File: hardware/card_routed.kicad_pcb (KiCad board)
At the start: 2 copper layers, 143 x 80 mm, 1 part

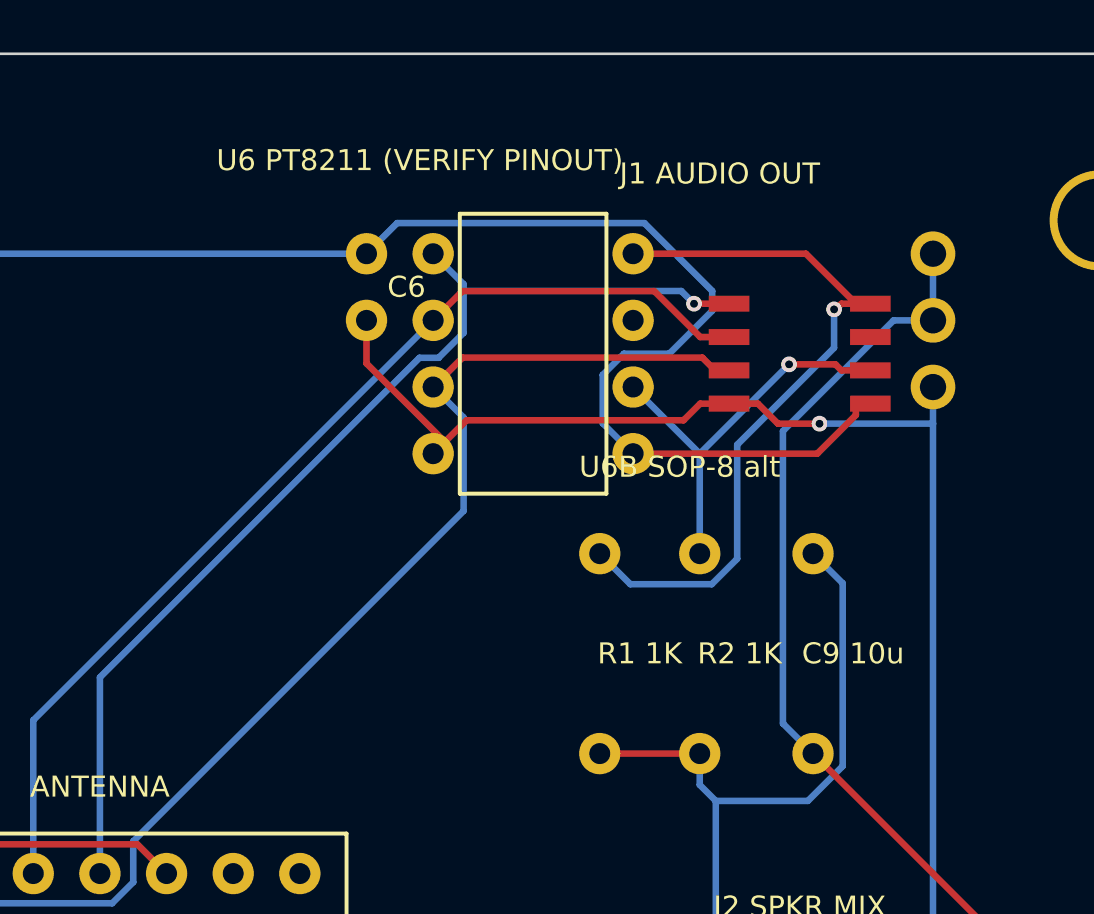
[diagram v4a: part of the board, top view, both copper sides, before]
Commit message: PT8211 datasheet in-tree; pinout verified and corrected
PT8211-S.pdf (Princeton Technology, v1.1) added to hardware/. The
flagged from-memory pinout was right on 6 of 8 pins: 6/8 were L/R
swapped (harmless — both sum to mono) and are now labeled truthfully
(6=LCH, 8=RCH, 7=NC). Datasheet also confirms both packages exist
(PT8211 DIP-8 / PT8211-S SO-8, matching our dual position) and that
the serial format is Japanese/LSB-justified, NOT standard I2S — noted
as a firmware requirement. 3.3V operation noted as Pico-ecosystem
practice vs the 5V nominal. Re-routed, DRC 0/0; fab package
regenerated. The last pre-order human check is closed.

Co-Authored-By: Claude Fable 5 <noreply@anthropic.com>
Claude-Session: https://claude.ai/code/session_01PB6zhL6oFB9zbtD4W85UDt
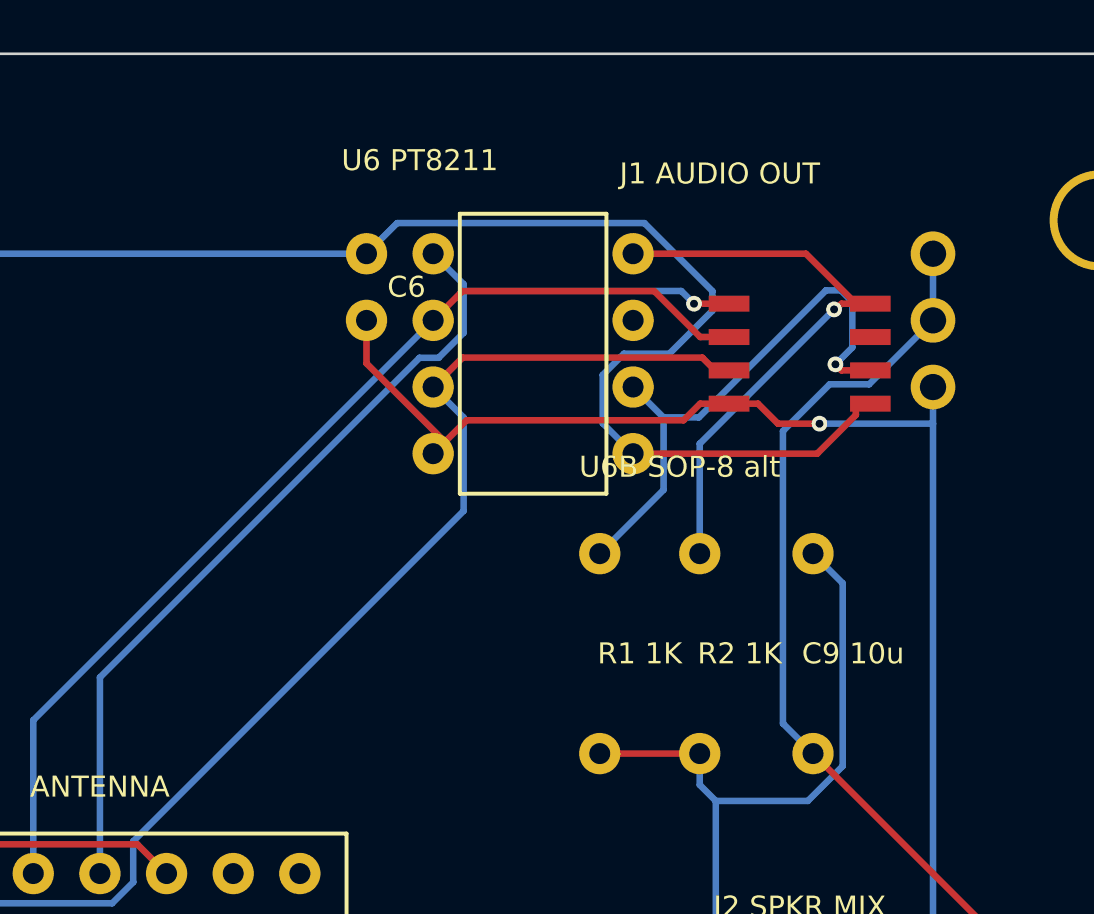
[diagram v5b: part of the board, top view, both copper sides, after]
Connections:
- ? pad 122: AOL -> AOR
- ? pad 126: AOR -> AOL
- ? pad 130: AOL -> AOR
- ? pad 134: AOR -> AOL
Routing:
- net AOR: track 15.4 -> 22.2 mm
- net AOL: track 27.9 -> 21.3 mm
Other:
- board text added: "U6 PT8211"
- board text removed: "U6 PT8211 (VERIFY PINOUT)"
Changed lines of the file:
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@@
     (pad "120" thru_hole circle (at 39.37 77.47) (size 1.5748 1.5748) (drill 0.8) (layers "*.Cu" "*.Mask"))
     (pad "121" thru_hole circle (at 102.87 7.62) (size 1.5748 1.5748) (drill 0.8) (layers "*.Cu" "*.Mask") (net 39 "BCK"))
-    (pad "122" thru_hole circle (at 110.49 7.62) (size 1.5748 1.5748) (drill 0.8) (layers "*.Cu" "*.Mask") (net 43 "AOL"))
+    (pad "122" thru_hole circle (at 110.49 7.62) (size 1.5748 1.5748) (drill 0.8) (layers "*.Cu" "*.Mask") (net 44 "AOR"))
     (pad "123" thru_hole circle (at 102.87 10.16) (size 1.5748 1.5748) (drill 0.8) (layers "*.Cu" "*.Mask") (net 40 "WS"))
     (pad "124" thru_hole circle (at 110.49 10.16) (size 1.5748 1.5748) (drill 0.8) (layers "*.Cu" "*.Mask"))
     (pad "125" thru_hole circle (at 102.87 12.7) (size 1.5748 1.5748) (drill 0.8) (layers "*.Cu" "*.Mask") (net 41 "DIN"))
-    (pad "126" thru_hole circle (at 110.49 12.7) (size 1.5748 1.5748) (drill 0.8) (layers "*.Cu" "*.Mask") (net 44 "AOR"))
+    (pad "126" thru_hole circle (at 110.49 12.7) (size 1.5748 1.5748) (drill 0.8) (layers "*.Cu" "*.Mask") (net 43 "AOL"))
     (pad "127" thru_hole circle (at 102.87 15.24) (size 1.5748 1.5748) (drill 0.8) (layers "*.Cu" "*.Mask") (net 1 "GND"))
     (pad "128" thru_hole circle (at 110.49 15.24) (size 1.5748 1.5748) (drill 0.8) (layers "*.Cu" "*.Mask") (net 3 "+3V3"))
     (pad "129" smd rect (at 114.1476 9.525) (size 1.5494 0.6096) (layers "F.Cu" "F.Mask" "F.Paste") (net 39 "BCK"))
-    (pad "130" smd rect (at 119.5324 9.525) (size 1.5494 0.6096) (layers "F.Cu" "F.Mask" "F.Paste") (net 43 "AOL"))
+    (pad "130" smd rect (at 119.5324 9.525) (size 1.5494 0.6096) (layers "F.Cu" "F.Mask" "F.Paste") (net 44 "AOR"))
     (pad "131" smd rect (at 114.1476 10.795) (size 1.5494 0.6096) (layers "F.Cu" "F.Mask" "F.Paste") (net 40 "WS"))
     (pad "132" smd rect (at 119.5324 10.795) (size 1.5494 0.6096) (layers "F.Cu" "F.Mask" "F.Paste"))
     (pad "133" smd rect (at 114.1476 12.065) (size 1.5494 0.6096) (layers "F.Cu" "F.Mask" "F.Paste") (net 41 "DIN"))
-    (pad "134" smd rect (at 119.5324 12.065) (size 1.5494 0.6096) (layers "F.Cu" "F.Mask" "F.Paste") (net 44 "AOR"))
+    (pad "134" smd rect (at 119.5324 12.065) (size 1.5494 0.6096) (layers "F.Cu" "F.Mask" "F.Paste") (net 43 "AOL"))
     (pad "135" smd rect (at 114.1476 13.335) (size 1.5494 0.6096) (layers "F.Cu" "F.Mask" "F.Paste") (net 1 "GND"))
     (pad "136" smd rect (at 119.5324 13.335) (size 1.5494 0.6096) (layers "F.Cu" "F.Mask" "F.Paste") (net 3 "+3V3"))
@@
   (gr_text "U5 HCT138" (at 31.242 56.134) (layer "F.SilkS") (effects (font (size 0.8 0.8) (thickness 0.15))))
   (gr_rect (start 103.886 6.096) (end 109.474 16.764) (layer "F.SilkS") (width 0.15) (fill none))
-  (gr_text "U6 PT8211 (VERIFY PINOUT)" (at 102.362 4.064) (layer "F.SilkS") (effects (font (size 0.8 0.8) (thickness 0.15))))
+  (gr_text "U6 PT8211" (at 102.362 4.064) (layer "F.SilkS") (effects (font (size 0.8 0.8) (thickness 0.15))))
   (gr_text "U6B SOP-8 alt" (at 112.268 15.748) (layer "F.SilkS") (effects (font (size 0.8 0.8) (thickness 0.15))))
   (gr_rect (start 47.752 29.718) (end 99.568 50.546) (layer "F.SilkS") (width 0.15) (fill none))
@@
   (segment (start 100.33 7.62) (end 101.4976 6.4524) (width 0.25) (layer "B.Cu") (net 3))
   (segment (start 101.4976 6.4524) (end 110.9206 6.4524) (width 0.25) (layer "B.Cu") (net 3))
-  (segment (start 110.9206 6.4524) (end 113.5053 9.0371) (width 0.25) (layer "B.Cu") (net 3))
-  (segment (start 113.5053 9.0371) (end 113.5053 9.7929) (width 0.25) (layer "B.Cu") (net 3))
-  (segment (start 113.5053 9.7929) (end 111.8682 11.43) (width 0.25) (layer "B.Cu") (net 3))
-  (segment (start 111.8682 11.43) (end 110.1415 11.43) (width 0.25) (layer "B.Cu") (net 3))
+  (segment (start 110.9206 6.4524) (end 113.5143 9.0461) (width 0.25) (layer "B.Cu") (net 3))
+  (segment (start 113.5143 9.0461) (end 113.5143 9.789) (width 0.25) (layer "B.Cu") (net 3))
+  (segment (start 113.5143 9.789) (end 111.8733 11.43) (width 0.25) (layer "B.Cu") (net 3))
+  (segment (start 111.8733 11.43) (end 110.1415 11.43) (width 0.25) (layer "B.Cu") (net 3))
   (segment (start 110.1415 11.43) (end 109.3323 12.2392) (width 0.25) (layer "B.Cu") (net 3))
   (segment (start 109.3323 12.2392) (end 109.3323 14.0823) (width 0.25) (layer "B.Cu") (net 3))
@@
   (segment (start 106.68 40.64) (end 91.948 40.64) (width 0.25) (layer "F.Cu") (net 42))
   (segment (start 91.948 40.64) (end 82.55 31.242) (width 0.25) (layer "F.Cu") (net 42))
-  (segment (start 109.22 19.05) (end 110.3843 20.2143) (width 0.25) (layer "B.Cu") (net 43))
-  (segment (start 110.3843 20.2143) (end 113.4886 20.2143) (width 0.25) (layer "B.Cu") (net 43))
-  (segment (start 113.4886 20.2143) (end 114.4563 19.2466) (width 0.25) (layer "B.Cu") (net 43))
-  (segment (start 114.4563 19.2466) (end 114.4563 14.9001) (width 0.25) (layer "B.Cu") (net 43))
-  (segment (start 114.4563 14.9001) (end 118.1496 11.2068) (width 0.25) (layer "B.Cu") (net 43))
-  (segment (start 118.1496 11.2068) (end 118.1496 9.7411) (width 0.25) (layer "B.Cu") (net 43))
-  (segment (start 118.9813 9.525) (end 117.0763 7.62) (width 0.25) (layer "F.Cu") (net 43))
-  (segment (start 117.0763 7.62) (end 110.49 7.62) (width 0.25) (layer "F.Cu") (net 43))
-  (segment (start 118.9813 9.525) (end 118.4306 9.525) (width 0.25) (layer "F.Cu") (net 43))
-  (segment (start 119.532 9.525) (end 118.9813 9.525) (width 0.25) (layer "F.Cu") (net 43))
-  (segment (start 118.1496 9.7411) (end 118.2145 9.7411) (width 0.25) (layer "F.Cu") (net 43))
-  (segment (start 118.2145 9.7411) (end 118.4306 9.525) (width 0.25) (layer "F.Cu") (net 43))
-  (via (at 118.1496 9.7411) (size 0.6) (drill 0.3) (layers "F.Cu" "B.Cu") (net 43))
-  (segment (start 118.4306 12.065) (end 118.2015 11.8359) (width 0.25) (layer "F.Cu") (net 44))
-  (segment (start 118.2015 11.8359) (end 116.4341 11.8359) (width 0.25) (layer "F.Cu") (net 44))
-  (segment (start 116.4341 11.8359) (end 113.03 15.24) (width 0.25) (layer "B.Cu") (net 44))
-  (segment (start 113.03 15.24) (end 110.49 12.7) (width 0.25) (layer "B.Cu") (net 44))
-  (segment (start 113.03 19.05) (end 113.03 15.24) (width 0.25) (layer "B.Cu") (net 44))
-  (segment (start 119.532 12.065) (end 118.4306 12.065) (width 0.25) (layer "F.Cu") (net 44))
-  (via (at 116.4341 11.8359) (size 0.6) (drill 0.3) (layers "F.Cu" "B.Cu") (net 44))
+  (segment (start 111.6498 13.8598) (end 110.49 12.7) (width 0.25) (layer "B.Cu") (net 43))
+  (segment (start 109.22 19.05) (end 111.6498 16.6202) (width 0.25) (layer "B.Cu") (net 43))
+  (segment (start 111.6498 16.6202) (end 111.6498 13.8598) (width 0.25) (layer "B.Cu") (net 43))
+  (segment (start 118.2015 11.8359) (end 118.8447 11.1927) (width 0.25) (layer "B.Cu") (net 43))
+  (segment (start 118.8447 11.1927) (end 118.8447 9.4528) (width 0.25) (layer "B.Cu") (net 43))
+  (segment (start 118.8447 9.4528) (end 118.4086 9.0167) (width 0.25) (layer "B.Cu") (net 43))
+  (segment (start 118.4086 9.0167) (end 117.8377 9.0167) (width 0.25) (layer "B.Cu") (net 43))
+  (segment (start 117.8377 9.0167) (end 112.9946 13.8598) (width 0.25) (layer "B.Cu") (net 43))
+  (segment (start 112.9946 13.8598) (end 111.6498 13.8598) (width 0.25) (layer "B.Cu") (net 43))
+  (segment (start 118.2015 11.8359) (end 118.4306 12.065) (width 0.25) (layer "F.Cu") (net 43))
+  (segment (start 119.532 12.065) (end 118.4306 12.065) (width 0.25) (layer "F.Cu") (net 43))
+  (via (at 118.2015 11.8359) (size 0.6) (drill 0.3) (layers "F.Cu" "B.Cu") (net 43))
+  (segment (start 118.9813 9.525) (end 117.0763 7.62) (width 0.25) (layer "F.Cu") (net 44))
+  (segment (start 117.0763 7.62) (end 110.49 7.62) (width 0.25) (layer "F.Cu") (net 44))
+  (segment (start 118.9813 9.525) (end 118.4306 9.525) (width 0.25) (layer "F.Cu") (net 44))
+  (segment (start 119.532 9.525) (end 118.9813 9.525) (width 0.25) (layer "F.Cu") (net 44))
+  (segment (start 113.03 19.05) (end 113.03 14.8607) (width 0.25) (layer "B.Cu") (net 44))
+  (segment (start 113.03 14.8607) (end 118.1496 9.7411) (width 0.25) (layer "B.Cu") (net 44))
+  (segment (start 118.1496 9.7411) (end 118.2145 9.7411) (width 0.25) (layer "F.Cu") (net 44))
+  (segment (start 118.2145 9.7411) (end 118.4306 9.525) (width 0.25) (layer "F.Cu") (net 44))
+  (via (at 118.1496 9.7411) (size 0.6) (drill 0.3) (layers "F.Cu" "B.Cu") (net 44))
   (segment (start 113.03 26.67) (end 109.22 26.67) (width 0.25) (layer "F.Cu") (net 45))
   (segment (start 113.6412 28.4741) (end 113.03 27.8629) (width 0.25) (layer "B.Cu") (net 45))
@@
   (segment (start 114.808 48.26) (end 113.6412 47.0932) (width 0.25) (layer "B.Cu") (net 45))
   (segment (start 113.6412 47.0932) (end 113.6412 28.4741) (width 0.25) (layer "B.Cu") (net 45))
-  (segment (start 117.348 26.67) (end 116.201 25.523) (width 0.25) (layer "B.Cu") (net 46))
-  (segment (start 116.201 25.523) (end 116.201 14.3766) (width 0.25) (layer "B.Cu") (net 46))
-  (segment (start 116.201 14.3766) (end 120.4176 10.16) (width 0.25) (layer "B.Cu") (net 46))
-  (segment (start 120.4176 10.16) (end 121.92 10.16) (width 0.25) (layer "B.Cu") (net 46))
+  (segment (start 121.92 10.16) (end 119.4849 12.5951) (width 0.25) (layer "B.Cu") (net 46))
+  (segment (start 119.4849 12.5951) (end 117.9825 12.5951) (width 0.25) (layer "B.Cu") (net 46))
+  (segment (start 117.9825 12.5951) (end 116.201 14.3766) (width 0.25) (layer "B.Cu") (net 46))
+  (segment (start 116.201 14.3766) (end 116.201 25.523) (width 0.25) (layer "B.Cu") (net 46))
+  (segment (start 116.201 25.523) (end 117.348 26.67) (width 0.25) (layer "B.Cu") (net 46))
   (segment (start 121.92 10.16) (end 121.92 7.62) (width 0.25) (layer "B.Cu") (net 46))
   (segment (start 125.73 34.29) (end 124.968 34.29) (width 0.25) (layer "F.Cu") (net 46))

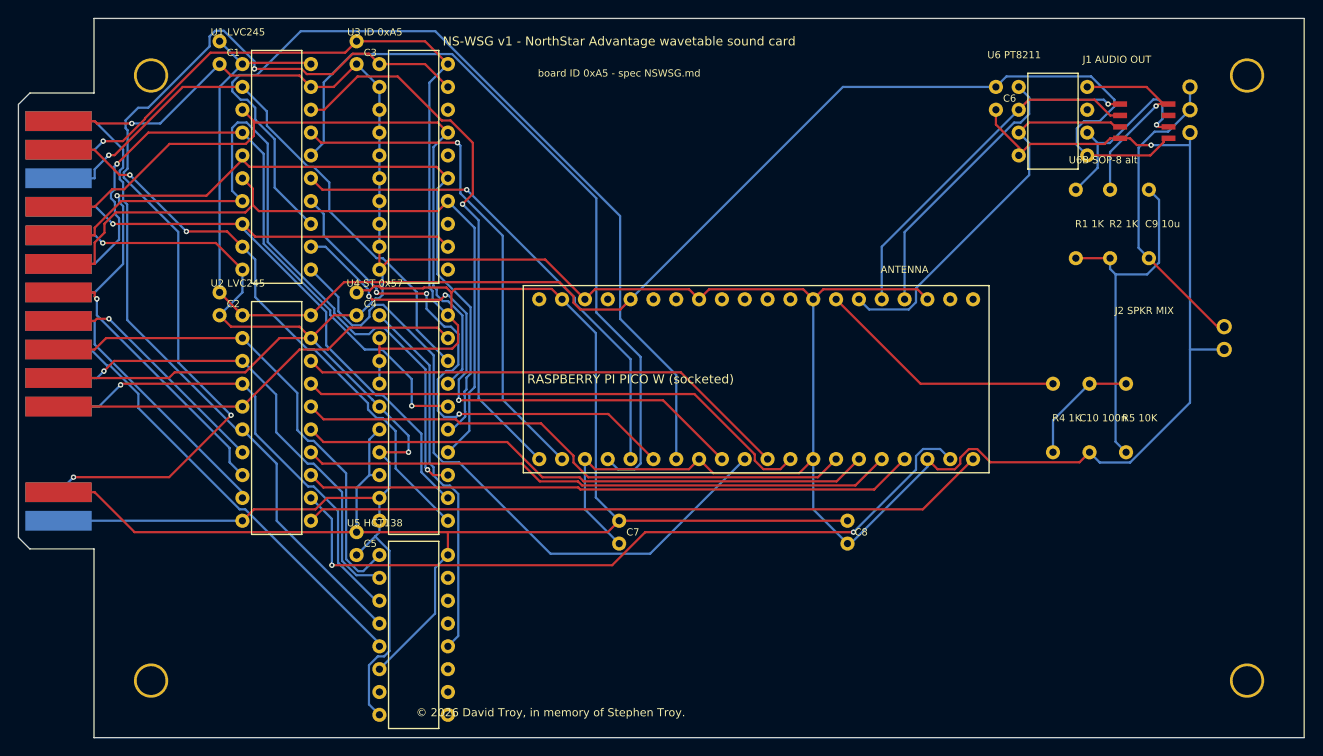
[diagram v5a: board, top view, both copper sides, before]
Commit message: On-board 3.5mm jack, stereo output per the PJRC PT8211 topology
Adopted the protosupplies/PJRC PT8211 adapter design: LCH/RCH each
through 47uF coupling to a real CUI SJ1-3523N TRS jack (footprint
taken from the KiCad-maintained library, rotated so the barrel
overhangs the right board edge) — true stereo replaces the mono sum,
so firmware can pan voices. VDD gets the datasheet's 10R + 47u + 100n
filter (new VDDF rail). PWM fallback and J2 mix-in re-plumbed to the
left channel. Fixed import_ses.py dropping wires for quoted net names
(underscored nets like AOL_C). Re-routed, DRC 0/0, fab package and
docs regenerated.

Co-Authored-By: Claude Fable 5 <noreply@anthropic.com>
Claude-Session: https://claude.ai/code/session_01PB6zhL6oFB9zbtD4W85UDt
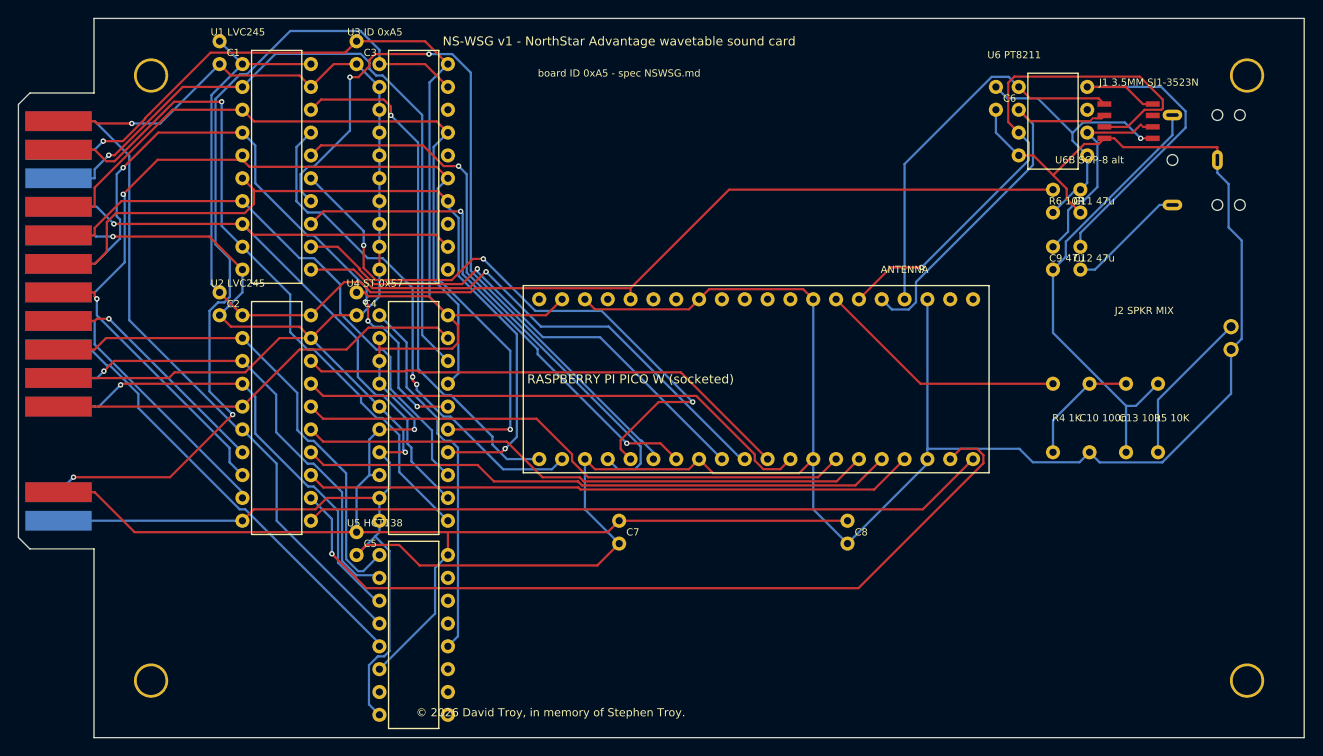
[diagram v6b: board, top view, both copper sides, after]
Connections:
- ? pad 122: AOR -> RCH
- ? pad 126: AOL -> LCH
- ? pad 128: +3V3 -> VDDF
- ? pad 130: AOR -> RCH
- ? pad 134: AOL -> LCH
- ? pad 136: +3V3 -> VDDF
- ? pad 177: AOL -> +3V3
- ? pad 178: ASUM -> VDDF
- ? pad 179: AOR -> VDDF
- ? pad 180: ASUM -> GND
- ? pad 181: ASUM -> LCH
- ? pad 182: AOUT -> AOL_C
- ? pad 183: PWM -> RCH
- ? pad 184: PWMF -> AOR_C
- ? pad 185: PWMF -> PWM
- ? pad 186: GND -> PWMF
- ? pad 188: ASUM -> GND
- ? pad 189: AOUT -> PWMF
- ? pad 190: AOUT -> AOL_C
- ? pad 191: GND -> AOL_C
- ? pad 192: AOUT -> J2SIG
- ? pad 193: GND -> (no net)
- ? pad 194: +3V3 -> (no net)
- ? pad 195: GND -> (no net)
- ? pad 196: +3V3 -> (no net)
- ? pad 197: GND -> (no net)
- ? pad 198: +5V -> J2SIG
- ? pad 200: +5V -> +3V3
- ? pad 202: +5V -> +3V3
- ? pad 204: +3V3 -> +5V
- ? pad 210: (no net) -> VDDF
- ? pad 211: (no net) -> GND
- ? pad 212: (no net) -> +5V
- ? pad 213: (no net) -> GND
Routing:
- net AOL_C: track 0.00 -> 51.0 mm
- net GP5: track 103.4 -> 56.9 mm, vias 0 -> 2
- net ASUM: track 40.1 -> 0.00 mm
- net RCH: track 0.00 -> 40.1 mm
- net AOUT: track 34.3 -> 0.00 mm
- net +3V3: track 172.9 -> 140.1 mm
- net VDDF: track 0.00 -> 32.2 mm, vias 0 -> 1
- net LCH: track 0.00 -> 23.4 mm
- net GP4: track 61.5 -> 84.2 mm, vias 3 -> 2
- net AOR: track 22.2 -> 0.00 mm, vias 1 -> 0
- net IO5: track 85.3 -> 63.8 mm, vias 1 -> 0
- net AOL: track 21.3 -> 0.00 mm, vias 1 -> 0
- net GP2: track 82.9 -> 63.7 mm, vias 0 -> 1
- net +5V: track 272.9 -> 254.1 mm, vias 1 -> 2
- net GND: track 479.0 -> 497.6 mm, vias 4 -> 3
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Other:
- board text added: "C11 47u"
- board text added: "C12 47u"
- board text added: "C13 10u"
- board text added: "C9 47u"
- board text added: "J1 3.5MM SJ1-3523N"
- board text added: "R6 10R"
- board text removed: "C9 10u"
- board text removed: "J1 AUDIO OUT"
- board text removed: "R1 1K"
- board text removed: "R2 1K"
